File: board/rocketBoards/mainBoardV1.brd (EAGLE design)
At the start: 38 x 15 mm, 47 parts

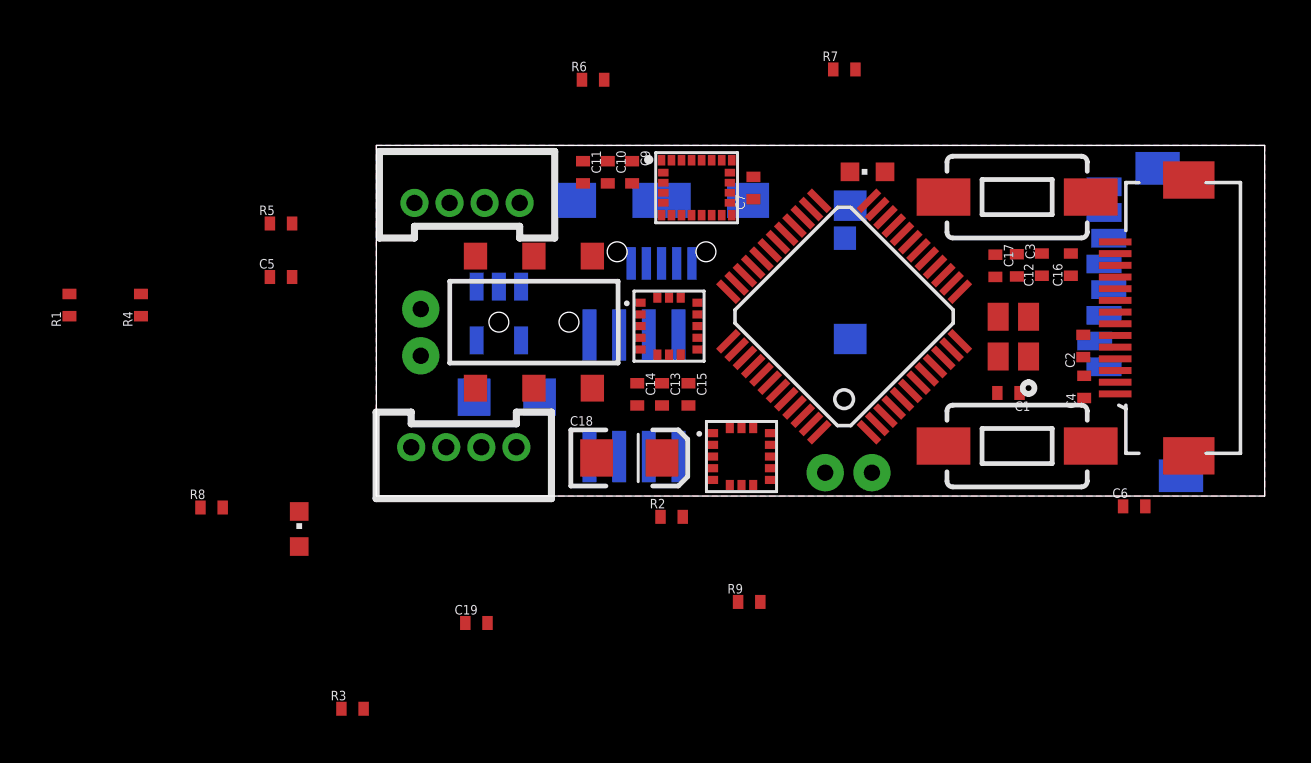
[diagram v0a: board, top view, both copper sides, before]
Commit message: Board layout done with autorouting
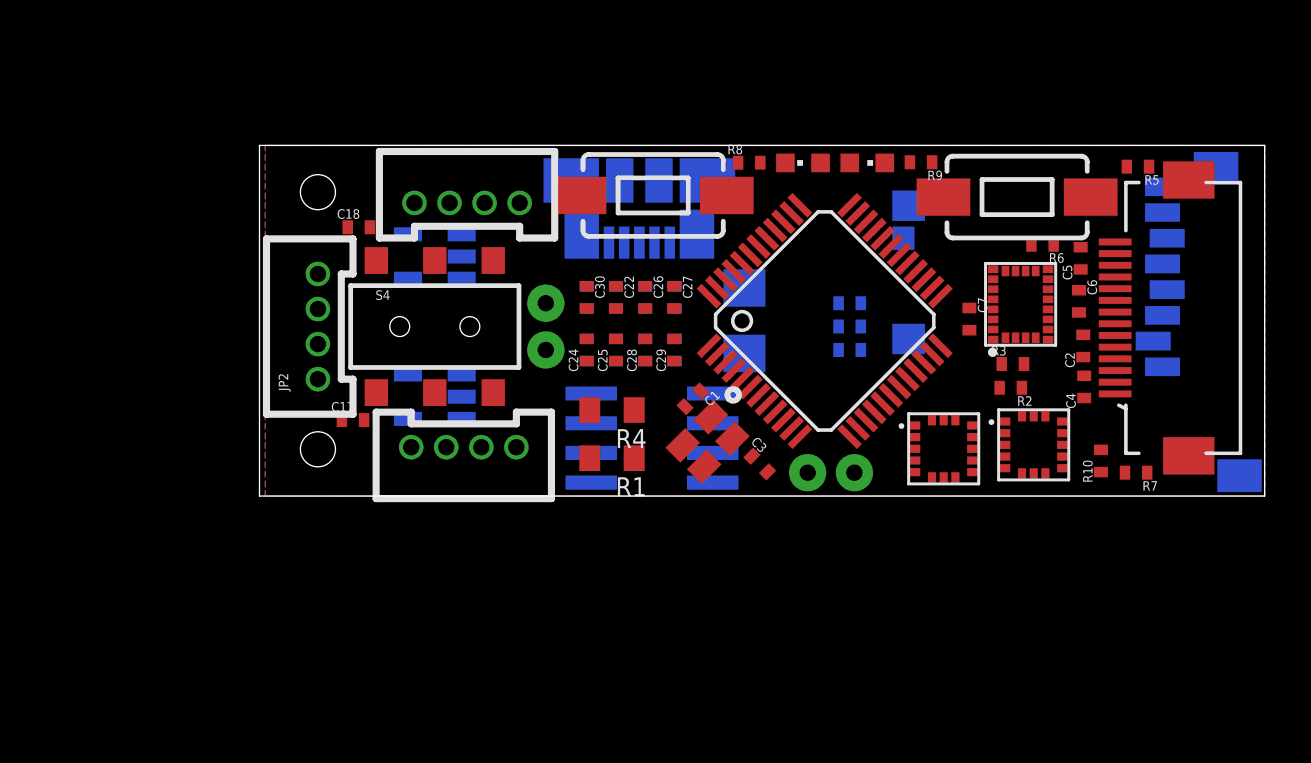
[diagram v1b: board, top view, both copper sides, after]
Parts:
- removed JP3: M02-JST-2-PTH-NO_SILK, SparkFun-Connectors:JST-2-PTH-NS
- removed JP4: USB_MICROB_PLUGCONN-11752, SparkFun-Connectors:USB-B-MICRO-SMD_V03
- removed S2: DPDT, SparkFun-Electromechanical:AYZ0202
- added C20, C22, C24, C25, C26: .1uF, ELL-i-Passives:C0402
- added C21: 100uF, ELL-i-Passives:C1206
- added C27, C28, C29, C30: .01uF, ELL-i-Passives:C0402
- added J1: 47346-0001, ELL-i-Connectors:MICRO_USB
- added JP2: (no value), SparkFun-Connectors:1X04-1.5MM_JST
- added JP8: M02-JST-2-PTH-NO_SILK, SparkFun-Connectors:JST-2-PTH-NS
- added R10: (no value), ELL-i-Passives:R0402
- added S4: DPDT, SparkFun-Electromechanical:AYZ0202
- added U$6: LDK220M33R, Sensors:SOT23-5
- C10, C14: value 1uF -> 10uF
- C11, C16: value 0.1uF -> .1uF
- C12, C13, C19, C9: value 10uF -> .1uF
- C15: value 1uF -> .1uF
- C17: value 0.1uF -> 1uF
- C18: value 10uF -> 1uF; device ELL-i-Passives:CT3216 -> ELL-i-Passives:C0402
- C8: device ELL-i-Passives:CT3216 -> ELL-i-Passives:C0402
- R1, R4: device ELL-i-Passives:R0402 -> ELL-i-Passives:R0805
- R6: value 33 -> 0
- R7: value 33 -> (none)
- moved R5 36.7 mm to (32.6, 14.1), turned to 180 degrees
- moved C5 34.2 mm to (30.1, 10.2), turned to 90 degrees
- moved R3 31.9 mm to (27.2, 5.65)
- moved C17 28.3 mm to (-1.00, 3.25), turned to 0 degrees
- moved R8 27.3 mm to (15.9, 14.3)
- moved LED1 26.6 mm to (18.2, 14.2), turned to 90 degrees
- moved R1 24.1 mm to (10.1, 1.62), turned to 180 degrees
- moved R7 21.3 mm to (32.5, 1.00), turned to 180 degrees
- moved C19 21.0 mm to (20.2, 8.25), flipped to the bottom, turned to 180 degrees
- moved R4 20.6 mm to (10.1, 3.68), turned to 180 degrees
- moved R6 20.5 mm to (28.5, 10.8), turned to 180 degrees
- moved R9 20.2 mm to (23.3, 14.3), turned to 180 degrees
- moved S1 18.9 mm to (11.8, 12.9), turned to 180 degrees
- moved 9-AXIS 17.9 mm to (29.1, 6.45), turned to 90 degrees
- moved C16 17.0 mm to (12.8, 8.50), flipped to the bottom, turned to 270 degrees
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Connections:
- removed net USB_FTOGGLE: S2.5, U1.4
- new net DRDY_M: 9-AXIS.9, U1.46
- new net LED_PIN2: LED1.A, U1.45
- new net N$20: JP8.1, S4.1
- new net N$21: R10.2, U$3.8
- new net PIO0_1: S4.5, U1.4
- new net SD_CD: U$3.9, U1.25
- net 3.3V: now also C19.1, C21.1, C22.1, C24.1, C25.1, C26.1, C27.1, C28.1, C29.1, C30.1, C8.1, JP2.1, R10.1, R6.2, R7.2, S4.6, U$6.5; no longer 9-AXIS.13, C17.1, C8.A, LED1.A, S2.6
- net GND: now also C18.2, C20.2, C21.2, C22.2, C24.2, C25.2, C26.2, C27.2, C28.2, C29.2, C30.2, C8.2, J1.GND, J1.P1, J1.P2, J1.P3, J1.P4, J1.P5, J1.P6, JP2.3, JP8.2, S4.4, U$6.2; no longer C18.C, C8.C, JP3.2, JP4.GND1, JP4.SHIELD1, JP4.SHIELD2, JP4.SHIELD3, S2.4
- net N$1: now also 9-AXIS.13, R6.1; no longer JP3.1, S2.1
- net N$14: now also 9-AXIS.24, C20.1; no longer R6.2, U1.20
- net N$15: now also J1.D+, U1.20; no longer JP4.D+1, R6.1
- net N$16: now also U$3.1; no longer JP4.D-1
- net N$17: now also J1.D-; no longer R7.2
- net SSP1_SSEL: now also U1.36; no longer U1.39
- net USB_VBUS: now also J1.VBUS, S4.3; no longer JP4.VBUS1, S2.3
- net VBUS: now also C17.1, C18.1, JP2.4, S4.2, U$6.1, U$6.3; no longer C18.A, C19.1, S2.2
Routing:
- added copper zone on layer 15, net 3.3V
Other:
- board size 38 x 15 mm -> 43 x 15 mm
